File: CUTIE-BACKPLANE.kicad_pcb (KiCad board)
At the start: 4 copper layers, 50.5 x 59.9 mm, 22 parts, among them J1 USB3_A, J2 ERF8-025-05.0-L-DV-L-K-TR, J3 ERF8-025-05.0-L-DV-L-K-TR, J4 ERF8-025-05.0-L-DV-L-K-TR

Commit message: push for fab
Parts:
- D1, D2, D3: footprint LED_SMD:LED_0603_1608Metric -> LED_SMD:LED_0805_2012Metric
- moved D3 0.20 mm to (110.0, 77.6)
- moved D2 0.10 mm to (99.0, 77.7)
- moved R3 0.10 mm to (87.0, 112.4)
- renumbered GND to GND1

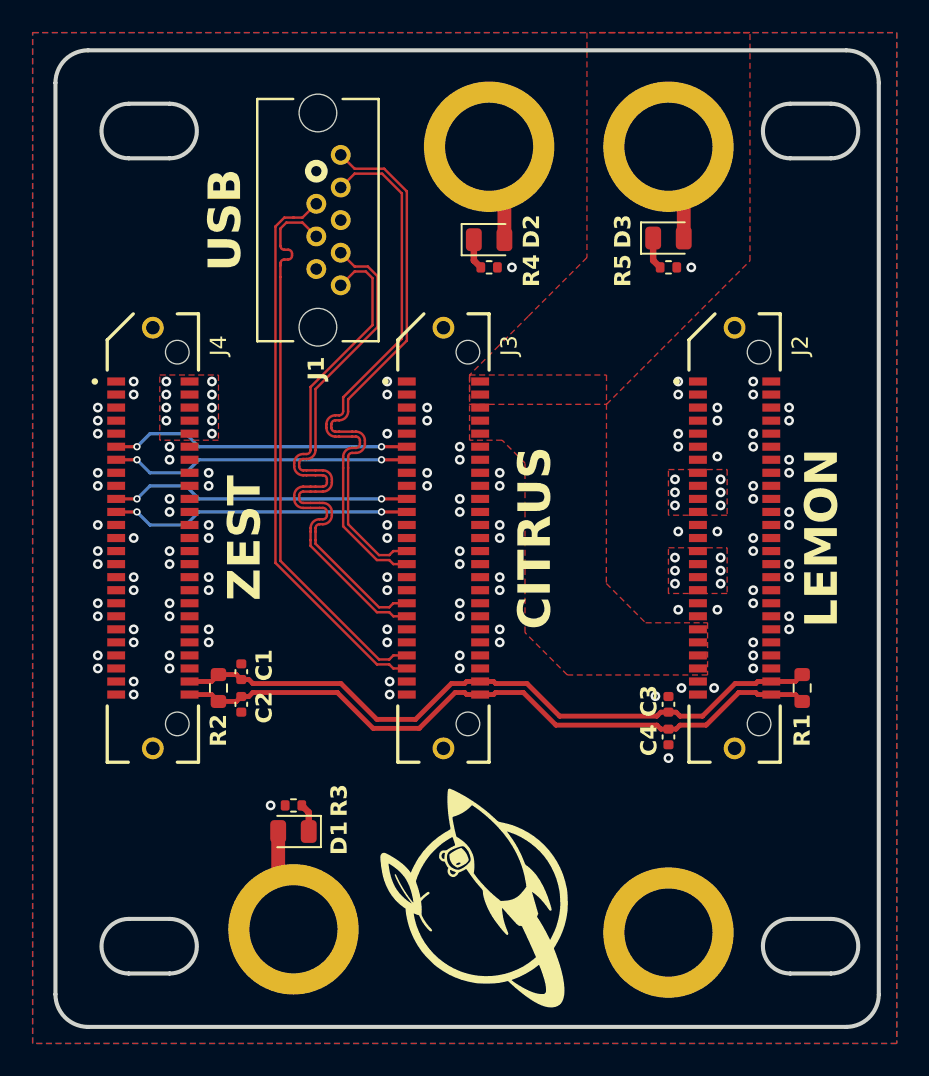
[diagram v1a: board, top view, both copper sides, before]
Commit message: rev b, flipped connectors
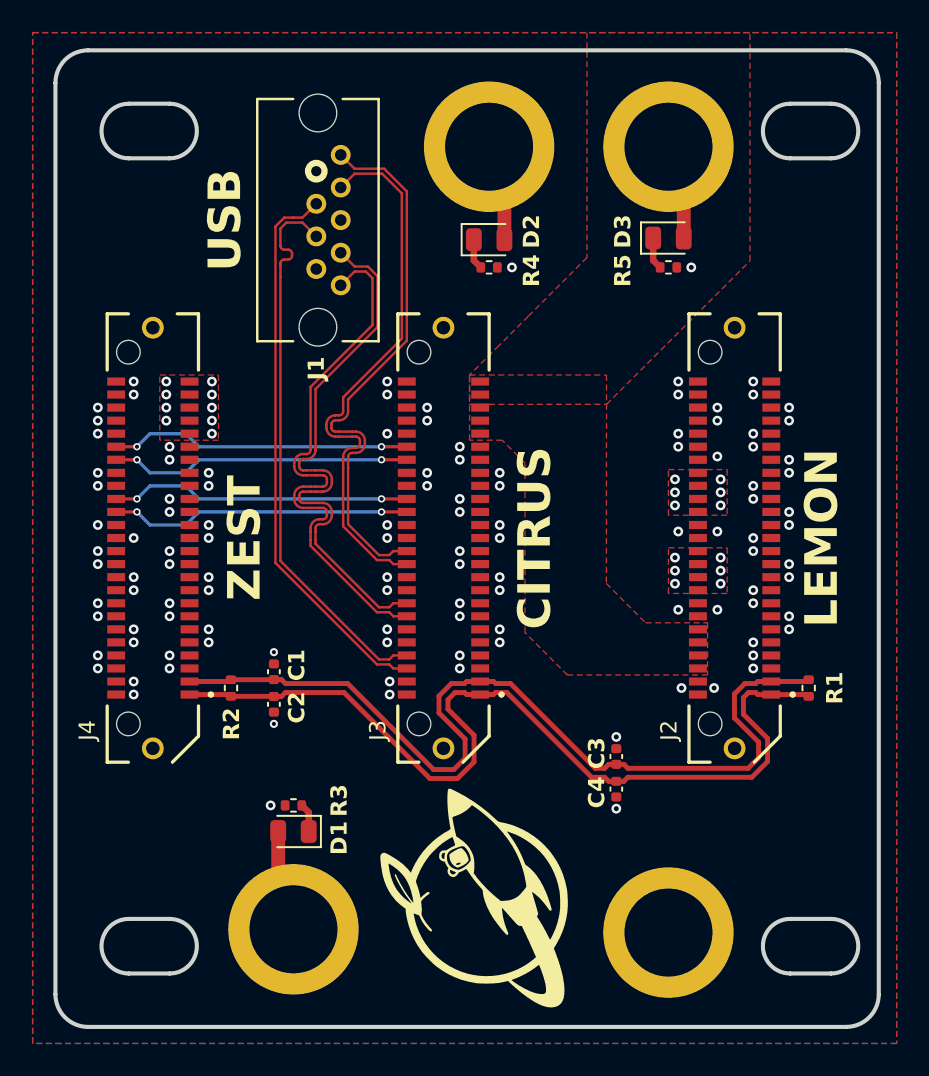
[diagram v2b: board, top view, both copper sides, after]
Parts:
- R1, R2: footprint Resistor_SMD:R_0603_1608Metric -> Resistor_SMD:R_0402_1005Metric
- moved C3 4.53 mm to (106.8, 109.4)
- moved C4 4.53 mm to (106.8, 111.4)
- moved C1 2.00 mm to (85.8, 104.2)
- moved C2 2.00 mm to (85.8, 106.2)
- moved R2 0.77 mm to (83.2, 105.2)
- moved R1 0.40 mm to (118.6, 105.2)
- turned J2 to -90 degrees
- turned J3 to -90 degrees
- turned J4 to -90 degrees
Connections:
- J2 pad 01: GND -> /CITRUS/CAN0.N
- J2 pad 03: GND -> /CITRUS/CAN0.P
- J2 pad 06: GND -> /CITRUS/5V0
- J2 pad 08: GND -> /CITRUS/5V0
- J2 pad 10: GND -> /CITRUS/5V0
- J2 pad 12: GND -> /CITRUS/5V0
- J2 pad 15: /LEMON/5VBUS3 -> GND
- J2 pad 17: /LEMON/5VBUS3 -> GND
- J2 pad 18: GND -> /LEMON/5VBUS2
- J2 pad 19: /LEMON/5VBUS3 -> GND
- J2 pad 20: GND -> /LEMON/5VBUS2
- J2 pad 21: /LEMON/5VBUS3 -> GND
- J2 pad 22: GND -> /LEMON/5VBUS2
- J2 pad 24: GND -> /LEMON/5VBUS2
- J2 pad 27: /LEMON/5VBUS2 -> GND
- J2 pad 29: /LEMON/5VBUS2 -> GND
- J2 pad 30: GND -> /LEMON/5VBUS3
- J2 pad 31: /LEMON/5VBUS2 -> GND
- J2 pad 32: GND -> /LEMON/5VBUS3
- J2 pad 33: /LEMON/5VBUS2 -> GND
- J2 pad 34: GND -> /LEMON/5VBUS3
- J2 pad 36: GND -> /LEMON/5VBUS3
- J2 pad 39: /CITRUS/5V0 -> GND
- J2 pad 41: /CITRUS/5V0 -> GND
- J2 pad 43: /CITRUS/5V0 -> GND
- J2 pad 45: /CITRUS/5V0 -> GND
- J2 pad 48: /CITRUS/CAN0.P -> GND
- J2 pad 50: /CITRUS/CAN0.N -> GND
- J3 pad 01: GND -> /CITRUS/CAN0.N
- J3 pad 02: /CITRUS/5V0 -> GND
- J3 pad 03: GND -> /CITRUS/CAN0.P
- J3 pad 04: /CITRUS/5V0 -> GND
- J3 pad 06: /CITRUS/5V0 -> /CITRUS/USB3.D_N
- J3 pad 08: /CITRUS/5V0 -> /CITRUS/USB3.D_P
- J3 pad 10: /CITRUS/5V0 -> GND
- J3 pad 11: /CITRUS/CMRF.CS0n -> GND
- J3 pad 13: /CITRUS/CMRF.SCLK -> GND
- J3 pad 14: GND -> /CITRUS/USB3.RX_N
- J3 pad 16: GND -> /CITRUS/USB3.RX_P
- J3 pad 19: /CITRUS/CMRF.MISO -> GND
- J3 pad 21: /CITRUS/CMRF.MOSI -> GND
- J3 pad 22: GND -> /CITRUS/USB3.TX_N
- J3 pad 24: GND -> /CITRUS/USB3.TX_P
- J3 pad 27: /CITRUS/USB3.TX_P -> GND
- J3 pad 29: /CITRUS/USB3.TX_N -> GND
- J3 pad 30: GND -> /CITRUS/CMRF.MOSI
- J3 pad 32: GND -> /CITRUS/CMRF.MISO
- J3 pad 35: /CITRUS/USB3.RX_P -> GND
- J3 pad 37: /CITRUS/USB3.RX_N -> GND
- J3 pad 38: GND -> /CITRUS/CMRF.SCLK
- J3 pad 40: GND -> /CITRUS/CMRF.CS0n
- J3 pad 41: GND -> /CITRUS/5V0
- J3 pad 43: /CITRUS/USB3.D_P -> /CITRUS/5V0
- J3 pad 45: /CITRUS/USB3.D_N -> /CITRUS/5V0
- J3 pad 47: GND -> /CITRUS/5V0
- J3 pad 48: /CITRUS/CAN0.P -> GND
- J3 pad 49: GND -> /CITRUS/5V0
- J3 pad 50: /CITRUS/CAN0.N -> GND
- J4 pad 01: GND -> /CITRUS/CAN0.N
- J4 pad 02: /LEMON/5VBUS3 -> GND
- J4 pad 03: GND -> /CITRUS/CAN0.P
- J4 pad 04: /LEMON/5VBUS3 -> GND
- J4 pad 06: /LEMON/5VBUS3 -> GND
- J4 pad 08: /LEMON/5VBUS3 -> GND
- J4 pad 10: /LEMON/5VBUS3 -> GND
- J4 pad 11: /CITRUS/CMRF.CS0n -> GND
- J4 pad 13: /CITRUS/CMRF.SCLK -> GND
- J4 pad 19: /CITRUS/CMRF.MISO -> GND
- J4 pad 21: /CITRUS/CMRF.MOSI -> GND
- J4 pad 30: GND -> /CITRUS/CMRF.MOSI
- J4 pad 32: GND -> /CITRUS/CMRF.MISO
- J4 pad 38: GND -> /CITRUS/CMRF.SCLK
- J4 pad 40: GND -> /CITRUS/CMRF.CS0n
- J4 pad 41: GND -> /LEMON/5VBUS3
- J4 pad 43: GND -> /LEMON/5VBUS3
- J4 pad 45: GND -> /LEMON/5VBUS3
- J4 pad 47: GND -> /LEMON/5VBUS3
- J4 pad 48: /CITRUS/CAN0.P -> GND
- J4 pad 49: GND -> /LEMON/5VBUS3
- J4 pad 50: /CITRUS/CAN0.N -> GND
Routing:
- net /CITRUS/CAN0.N: track 42.0 -> 56.1 mm
- net /CITRUS/CAN0.P: track 42.0 -> 56.1 mm
- net GND: vias 113 -> 115
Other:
- board text added: "B"
- board text removed: "A"

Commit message: mechanical spacing
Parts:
- moved J1 0.70 mm to (89.1, 73.5)
- renumbered GND1 to GND
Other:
- board text added: "hsp payload apr 2026"
